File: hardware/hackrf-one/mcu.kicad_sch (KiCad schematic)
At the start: 132 parts, among them J1 USB-MICRO-B, P1 1V8, P20 GPIO, P22 I2S, P23 DBGEN, P24 TRST, P25 LPC_ISP, P26 LPC_JTAG, P28 SD, P29 CPLD_JTAG, P3 GND, P30 BANK2_AUX, P5 LEDS, P68 SPIFI_CS, P69 VREGMODE, P70 EN_1V8, P71 ID, P72 GP_CLKIN, P73 P1_2, P74 P1_1, P75 GP_CLKIN, P76 GP_CLKIN, P77 GP_CLKIN, P78 GP_CLKIN, P79 GP_CLKIN, P8 VCC, P80 SHIELD, P81 SPIFI_SIO2, P82 SPIFI_SIO3, Q5 MOSFET_P, SW1 DFU, SW2 RESET, U15 USB6B1, U20 W25Q80, U21 TPS62410, U23 LPC4320FBD144, U24 GSG-XC2C64A-7VQG100C, X2 MCU_XTAL, X3 RTC_XTAL

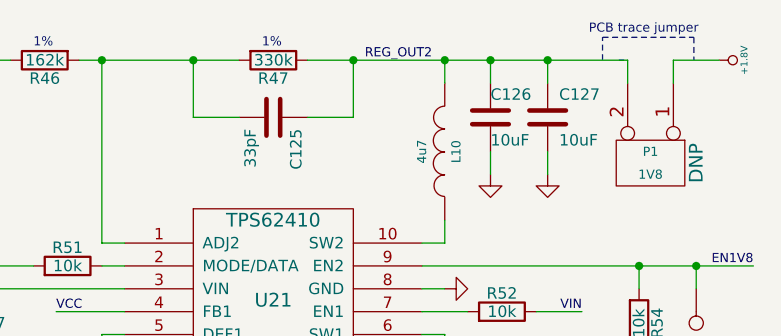
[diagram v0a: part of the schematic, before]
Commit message: Fixed minor DRCs
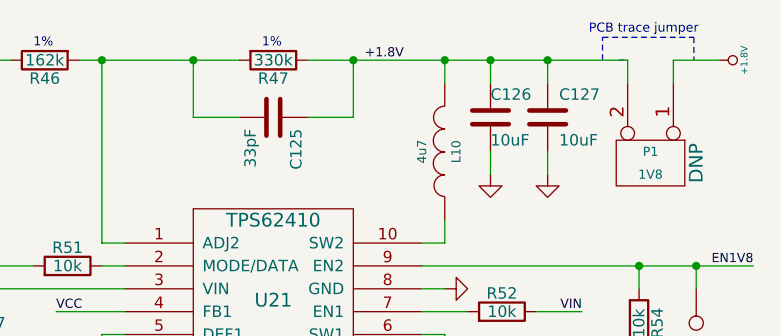
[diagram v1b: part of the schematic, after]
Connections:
- net REG_OUT2 is gone; now on net +1.8V: C125.1, C126.1, C127.1, L10.2, P1.2 (PM), R47.1
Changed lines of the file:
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@@
 		)
 	)
-	(label "REG_OUT2"
+	(label "+1.8V"
 		(at 373.38 17.78 0)
 		(fields_autoplaced yes)

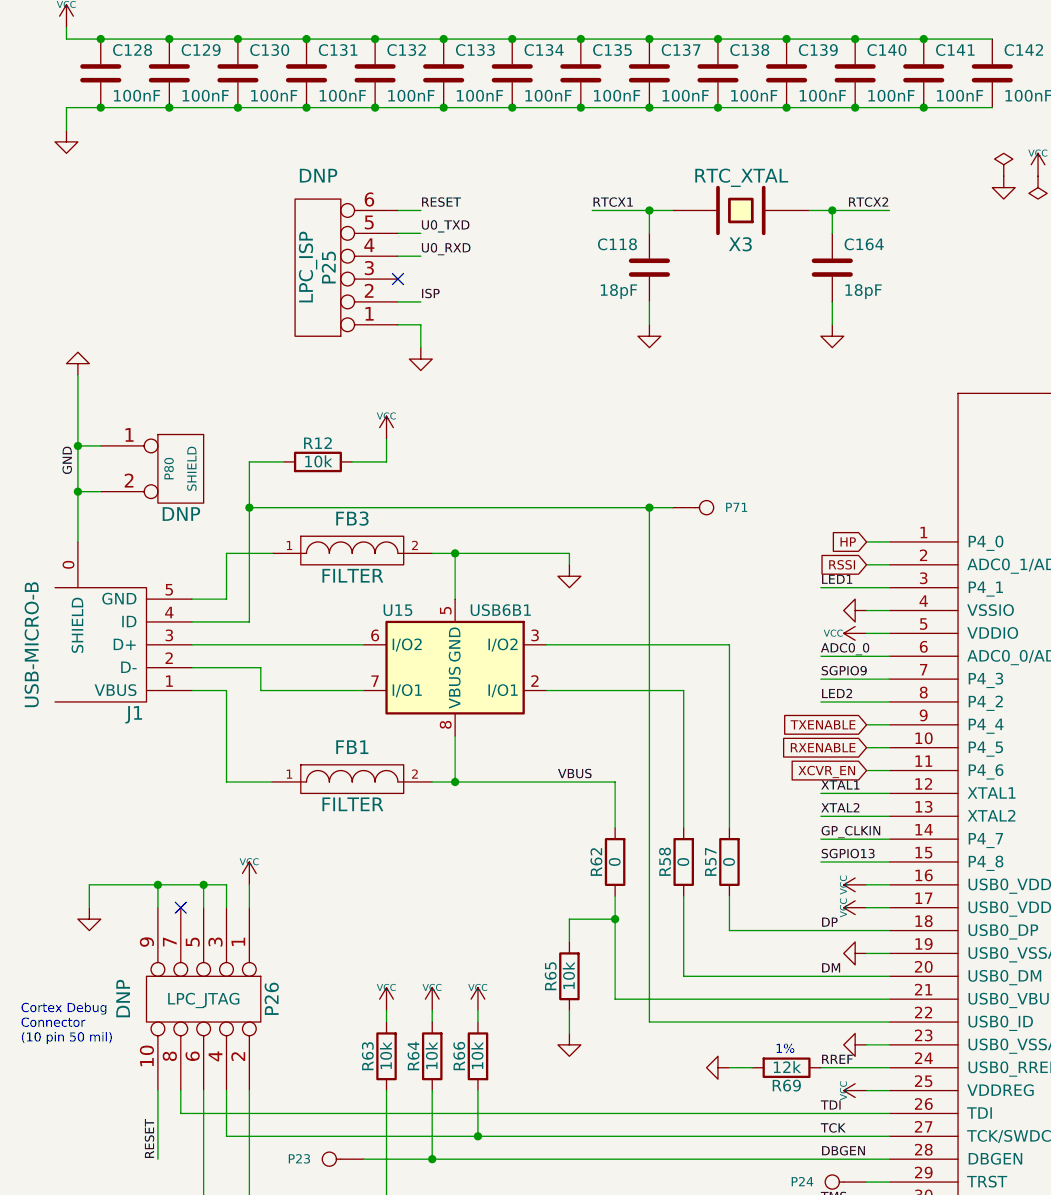
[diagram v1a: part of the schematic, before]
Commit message: Changed to USB-C connector
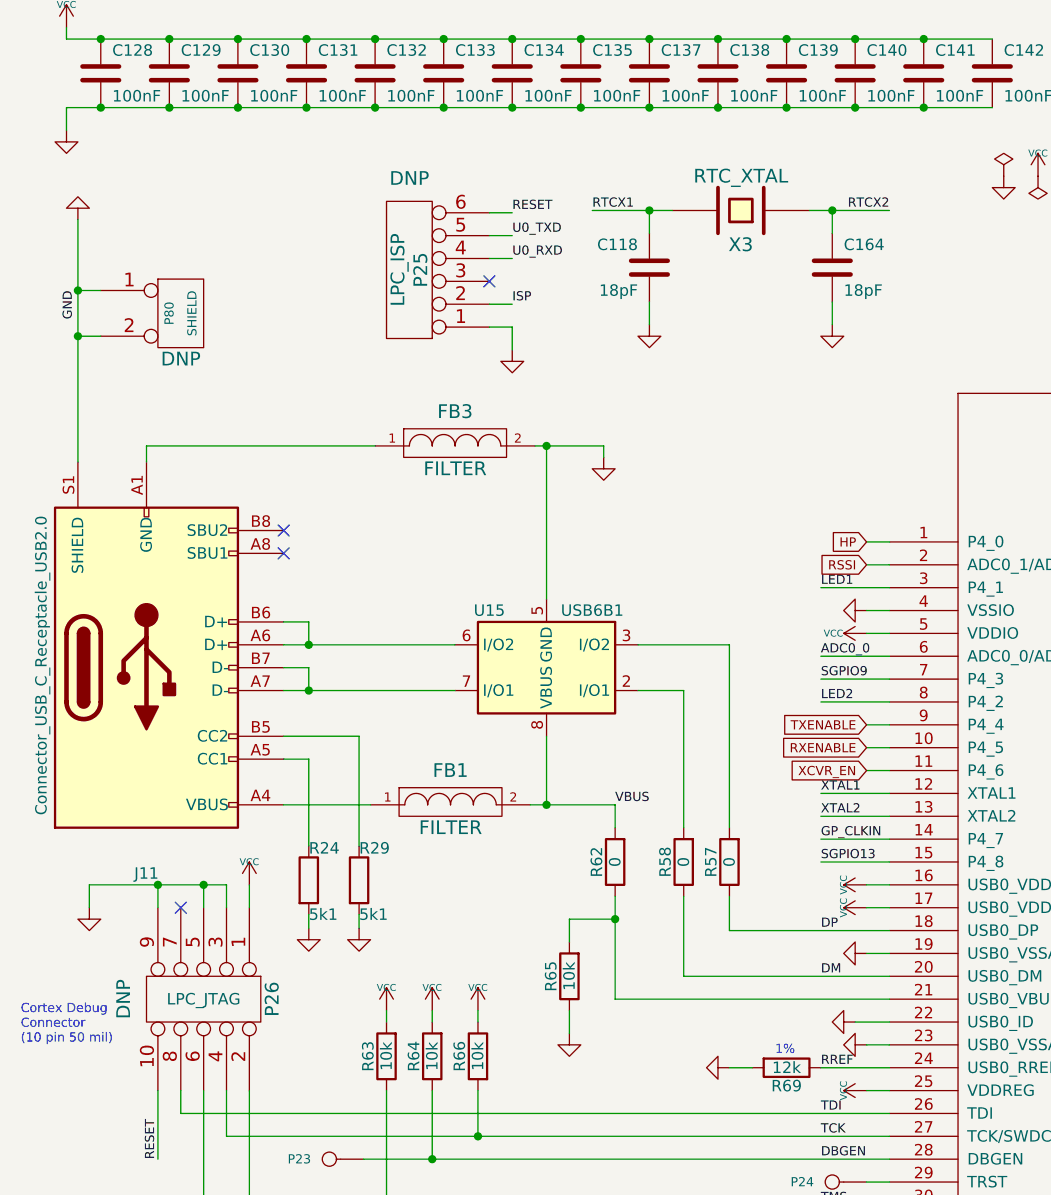
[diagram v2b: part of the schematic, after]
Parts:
- removed J1: USB-MICRO-B, hackrf:GSG-USB-MICROB-FCI-10103592-EXT, symbol hackrf-one:GSG-USB-MICRO-B-SHIELDED-hackrf
- removed P71: ID, hackrf:GSG-TESTPOINT-50MIL, symbol hackrf-one:CONN_1-hackrf
- removed R12: 10k, hackrf:GSG-0402, symbol Device:R
- added J11: Connector_USB_C_Receptacle_USB2.0, gsg-modules:USB-C_SMD-TYPE-C-31-M-12, symbol gsg-kicad-lib:USB_C_Receptacle_USB2.0-Connector
- added R24, R29: 5k1, hackrf:GSG-0402, symbol Device:R
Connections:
- net GND: now also U23.22 (USB0_ID), J11.S1 (SHIELD), R24.2, R29.2
- net at FB1.1: now also J11.A4 (VBUS), J11.A9 (VBUS), J11.B4 (VBUS), J11.B9 (VBUS)
- net at U15.7 (I/O1): now also J11.A7 (D-), J11.B7 (D-)
- net at U15.6 (I/O2): now also J11.A6 (D+), J11.B6 (D+)
- net at FB3.1: now also J11.A1 (GND), J11.A12 (GND), J11.B1 (GND), J11.B12 (GND)
- new net: J11.A5 (CC1), R24.1
- new net: J11.B5 (CC2), R29.1
- no-connect marks 18 -> 20
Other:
- moved on the sheet: FB1, FB3, P25, P80, U15

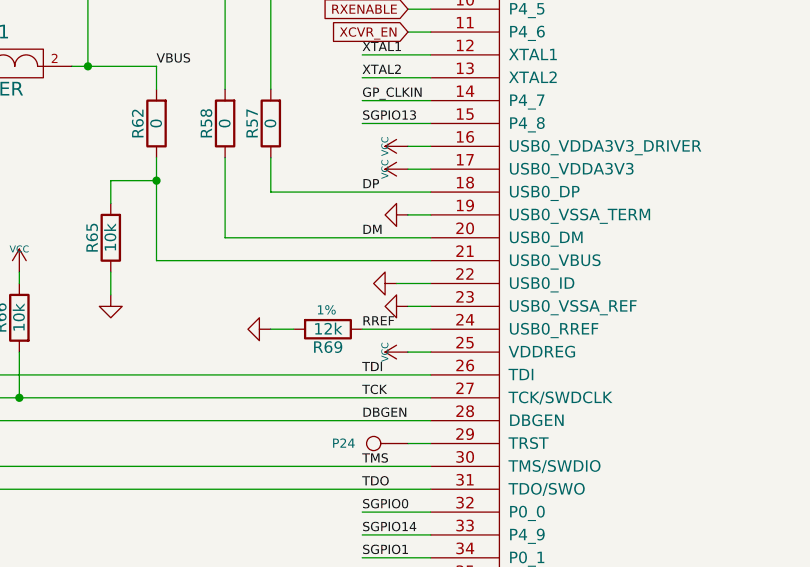
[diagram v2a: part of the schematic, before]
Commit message: Leave ID pin open, to signal it's a USB device
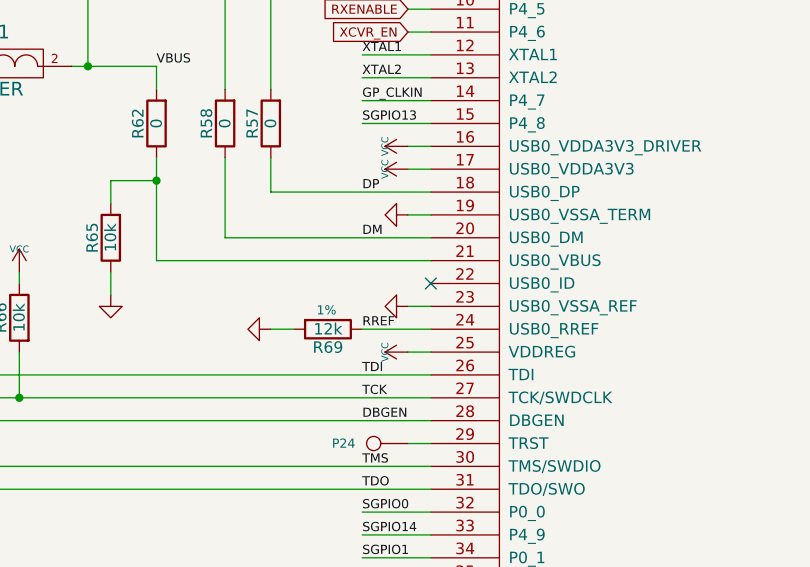
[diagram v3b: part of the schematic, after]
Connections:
- net GND: no longer U23.22 (USB0_ID)
- no-connect marks 20 -> 21
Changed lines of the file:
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@@
 	)
 	(no_connect
+		(at 109.22 129.54)
+	)
+	(no_connect
 		(at 246.38 124.46)
 	)
@@
 	(wire
 		(pts
-			(xy 105.41 129.54) (xy 109.22 129.54)
-		)
-		(stroke
-			(width 0)
-			(type default)
-		)
-	)
-	(wire
-		(pts
 			(xy 97.79 209.55) (xy 104.14 209.55)
 		)
@@
 					(unit 1)
 				)
-			)
-		)
-	)
-	(symbol
-		(lib_id "hackrf-one:GND-power")
-		(at 105.41 129.54 270)
-		(unit 1)
-		(exclude_from_sim no)
-		(in_bom yes)
-		(on_board yes)
-		(dnp no)
-		(property "Reference" "#PWR013"
-			(at 105.41 129.54 0)
-			(effects
-				(font
-					(size 0.762 0.762)
-				)
-				(hide yes)
-			)
-		)
-		(property "Value" "GND"
-			(at 103.632 129.54 0)
-			(effects
-				(font
-					(size 0.762 0.762)
-				)
-				(hide yes)
-			)
-		)
-		(property "Footprint" ""
-			(at 105.41 129.54 0)
-			(effects
-				(font
-					(size 1.524 1.524)
-				)
-				(hide yes)
-			)
-		)
-		(property "Datasheet" ""
-			(at 105.41 129.54 0)
-			(effects
-				(font
-					(size 1.524 1.524)
-				)
-				(hide yes)
-			)
-		)
-		(property "Description" ""
-			(at 105.41 129.54 0)
-			(effects
-				(font
-					(size 1.27 1.27)
-				)
-				(hide yes)
-			)
-		)
-		(pin "1"
-		)
-		(instances
-			(project "hackrf-one"
-				(path "/00e5afbc-cf8c-40e8-b378-e4fd9cf88403/00000000-0000-0000-0000-00005037043e"
-					(reference "#PWR013")
-					(unit 1)
-				)

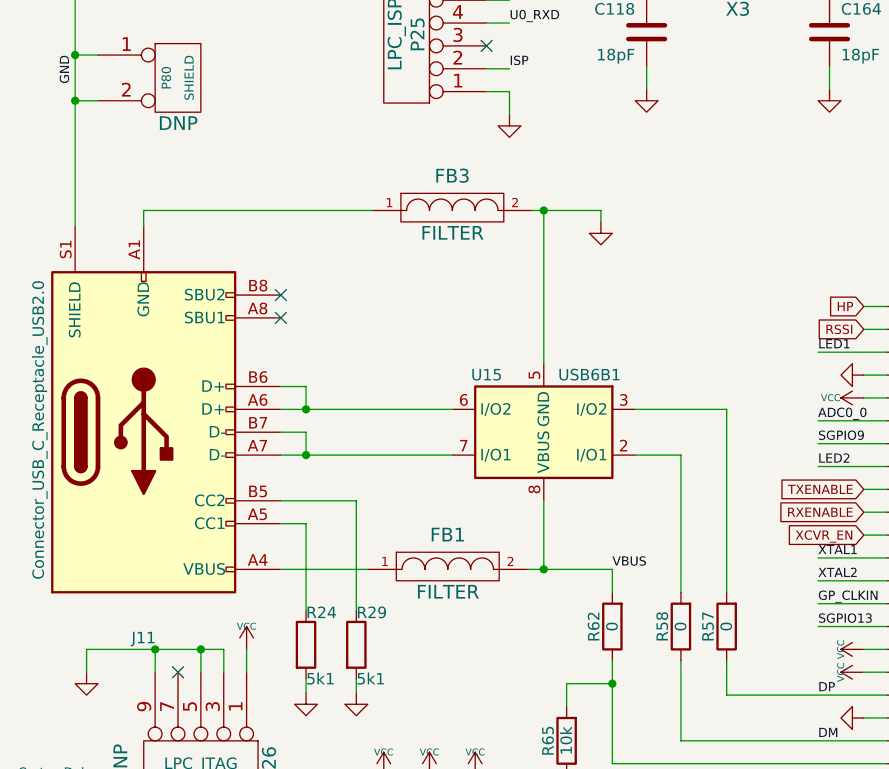
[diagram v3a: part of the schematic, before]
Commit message: Change USB protection to ECMF02-4CMX8
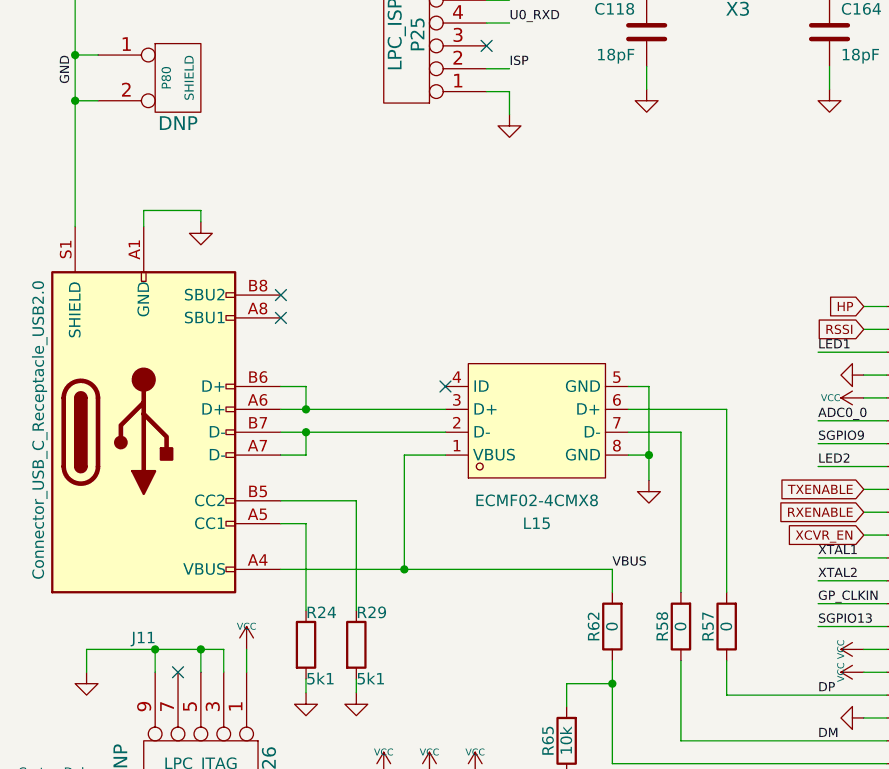
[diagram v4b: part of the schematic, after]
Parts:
- removed FB1, FB3: FILTER, hackrf:GSG-0805, symbol hackrf-one:FILTER-hackrf
- removed U15: USB6B1, Package_SO:SOIC-8_3.9x4.9mm_P1.27mm, symbol Power_Protection:USB6B1
- added L15: ECMF02-4CMX8, gsg-modules:QFN-8_L2.5-W1.2-P0.50-BL, symbol gsg-kicad-lib:ECMF02-4CMX8
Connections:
- net GND: now also J11.A1 (GND), J11.A12 (GND), J11.B1 (GND), J11.B12 (GND), L15.5 (GND), L15.8 (GND)
- net VBUS: now also J11.A4 (VBUS), J11.A9 (VBUS), J11.B4 (VBUS), J11.B9 (VBUS), L15.1 (VBUS)
- net at R57.2: now also L15.6 (D+)
- net at R58.2: now also L15.7 (D-)
- net at J11.A6 (D+), J11.B6 (D+): now also L15.3 (D+)
- net at J11.A7 (D-), J11.B7 (D-): now also L15.2 (D-)
- no-connect marks 21 -> 22

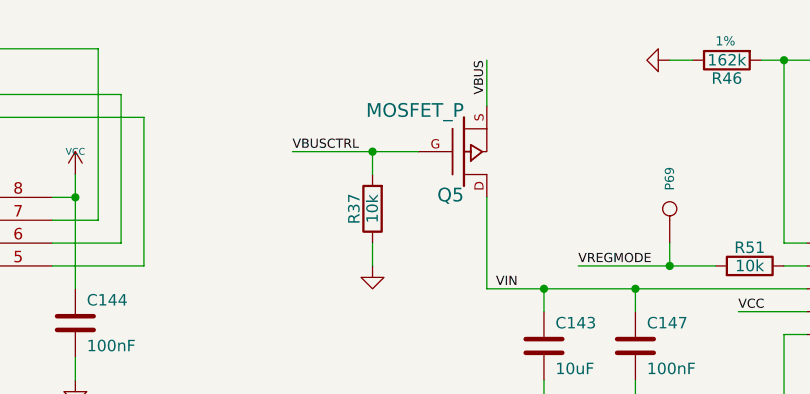
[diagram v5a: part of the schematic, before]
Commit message: Updated to move USB-C connector to save location as OpenSourceSDRLab's R10C
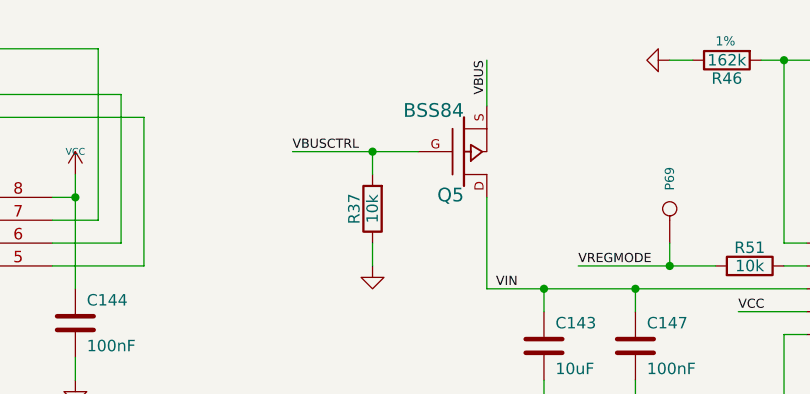
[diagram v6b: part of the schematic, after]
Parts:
- Q5: value MOSFET_P -> BSS84
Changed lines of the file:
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@@
 			)
 		)
-		(property "Value" "MOSFET_P"
+		(property "Value" "BSS84"
 			(at 308.61 23.368 0)
 			(effects
